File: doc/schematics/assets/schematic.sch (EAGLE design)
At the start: 3 parts

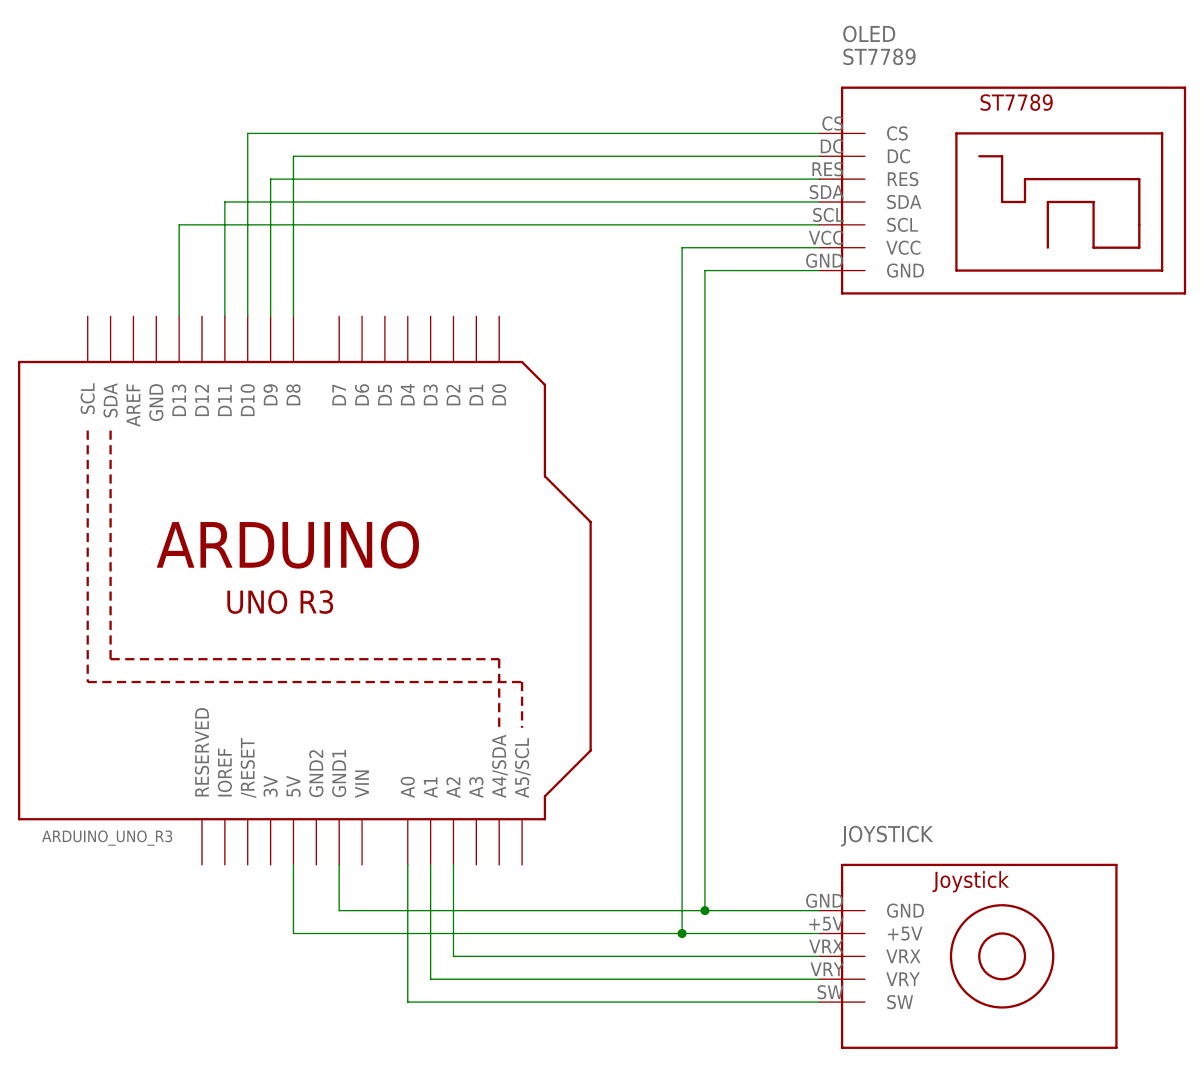
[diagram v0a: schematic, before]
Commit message: doc: Update schematic to new pin assignment.
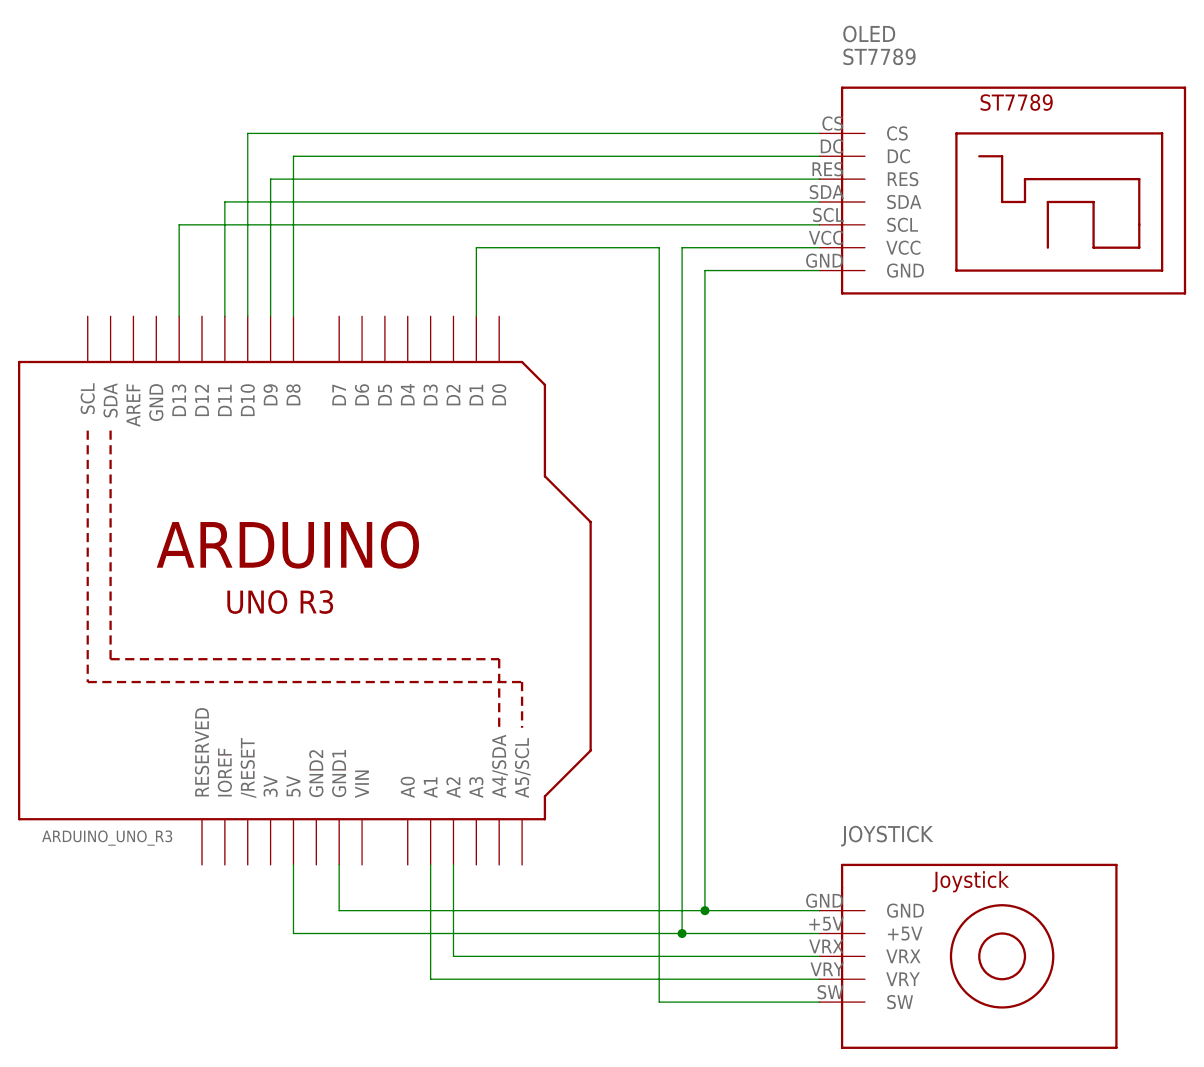
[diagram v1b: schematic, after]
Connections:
- net N$6: now also ARDUINO_UNO_R3.D1; no longer ARDUINO_UNO_R3.A0
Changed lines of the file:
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@@
 <net name="N$6" class="0">
 <segment>
+<pinref part="ARDUINO_UNO_R3" gate="G$1" pin="D1"/>
+<wire x1="50.8" y1="66.04" x2="50.8" y2="73.66" width="0.1524" layer="91"/>
+<wire x1="50.8" y1="73.66" x2="71.12" y2="73.66" width="0.1524" layer="91"/>
+<wire x1="71.12" y1="73.66" x2="71.12" y2="-10.16" width="0.1524" layer="91"/>
 <pinref part="JOYSTICK" gate="G$1" pin="SW"/>
-<wire x1="88.9" y1="-10.16" x2="43.18" y2="-10.16" width="0.1524" layer="91"/>
-<pinref part="ARDUINO_UNO_R3" gate="G$1" pin="A0"/>
-<wire x1="43.18" y1="-10.16" x2="43.18" y2="5.08" width="0.1524" layer="91"/>
+<wire x1="71.12" y1="-10.16" x2="88.9" y2="-10.16" width="0.1524" layer="91"/>
 </segment>
 </net>
